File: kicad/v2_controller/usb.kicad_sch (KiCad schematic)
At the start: 23 parts, among them J3 USB_C_Receptacle_USB2.0, J4 USB_C_Receptacle_USB2.0, U4 NCP167BMX330TBG, U5 USBLC6-2P6, U6 USBLC6-2P6, U7 CP2102N-Axx-xQFN24

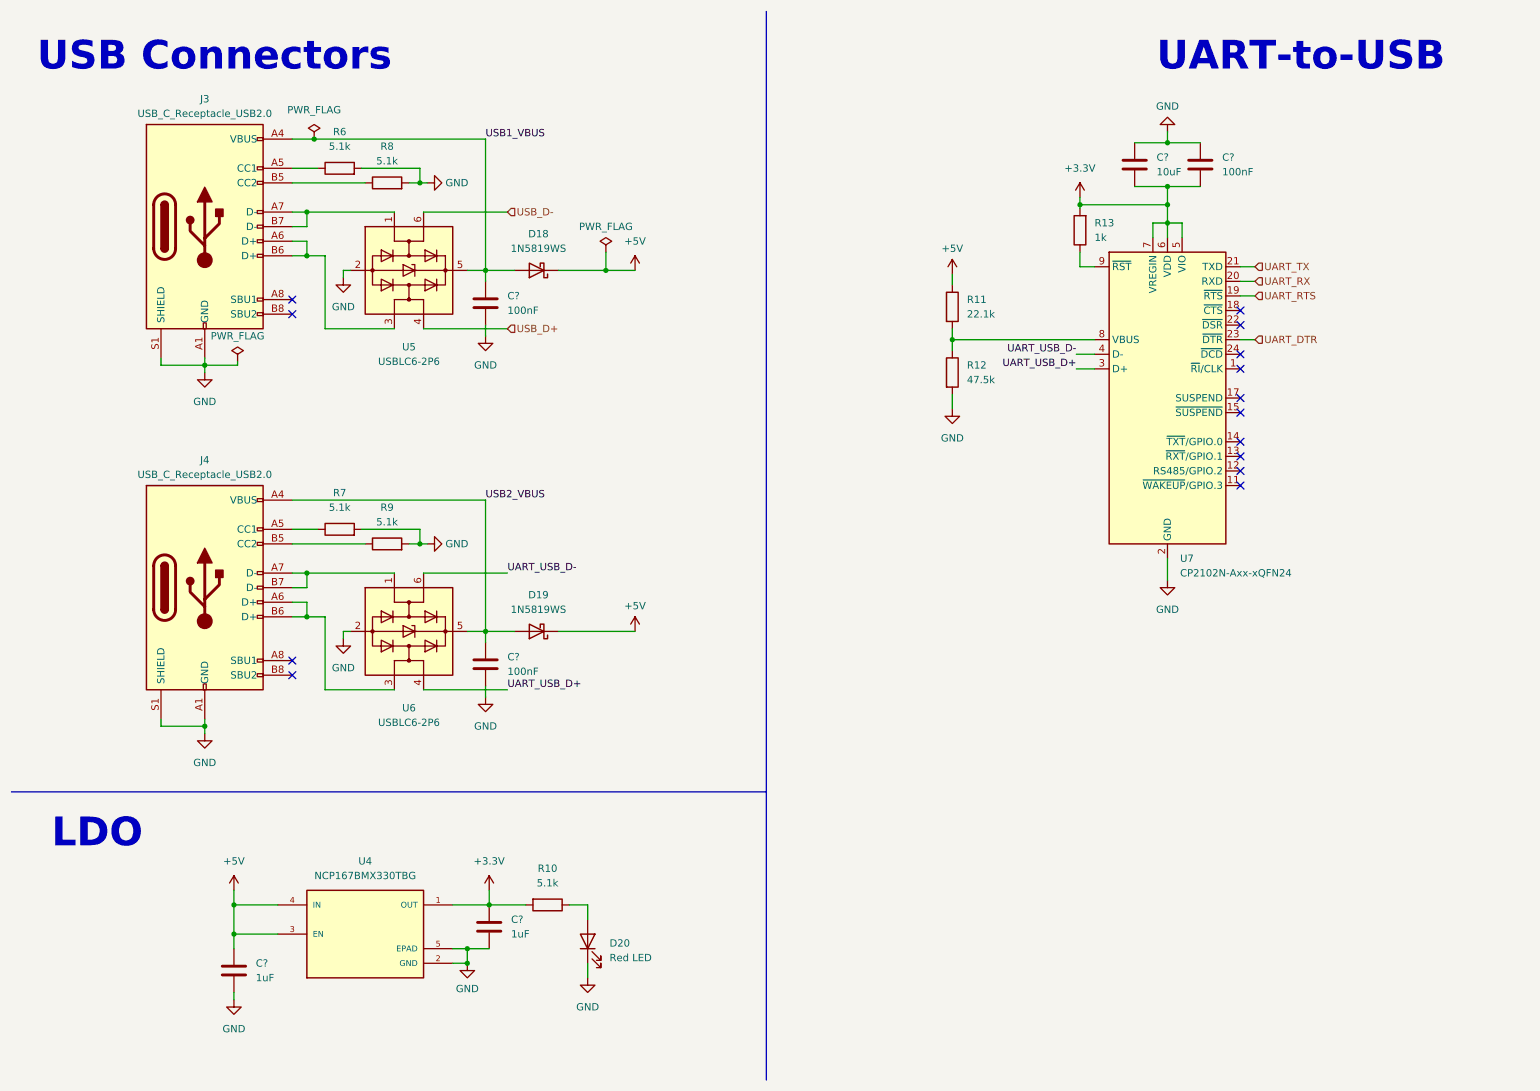
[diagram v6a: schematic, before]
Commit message: [kicad] finish initial component placement
This will probably need to be tweaked further once I begin routing,
but is a start for now.
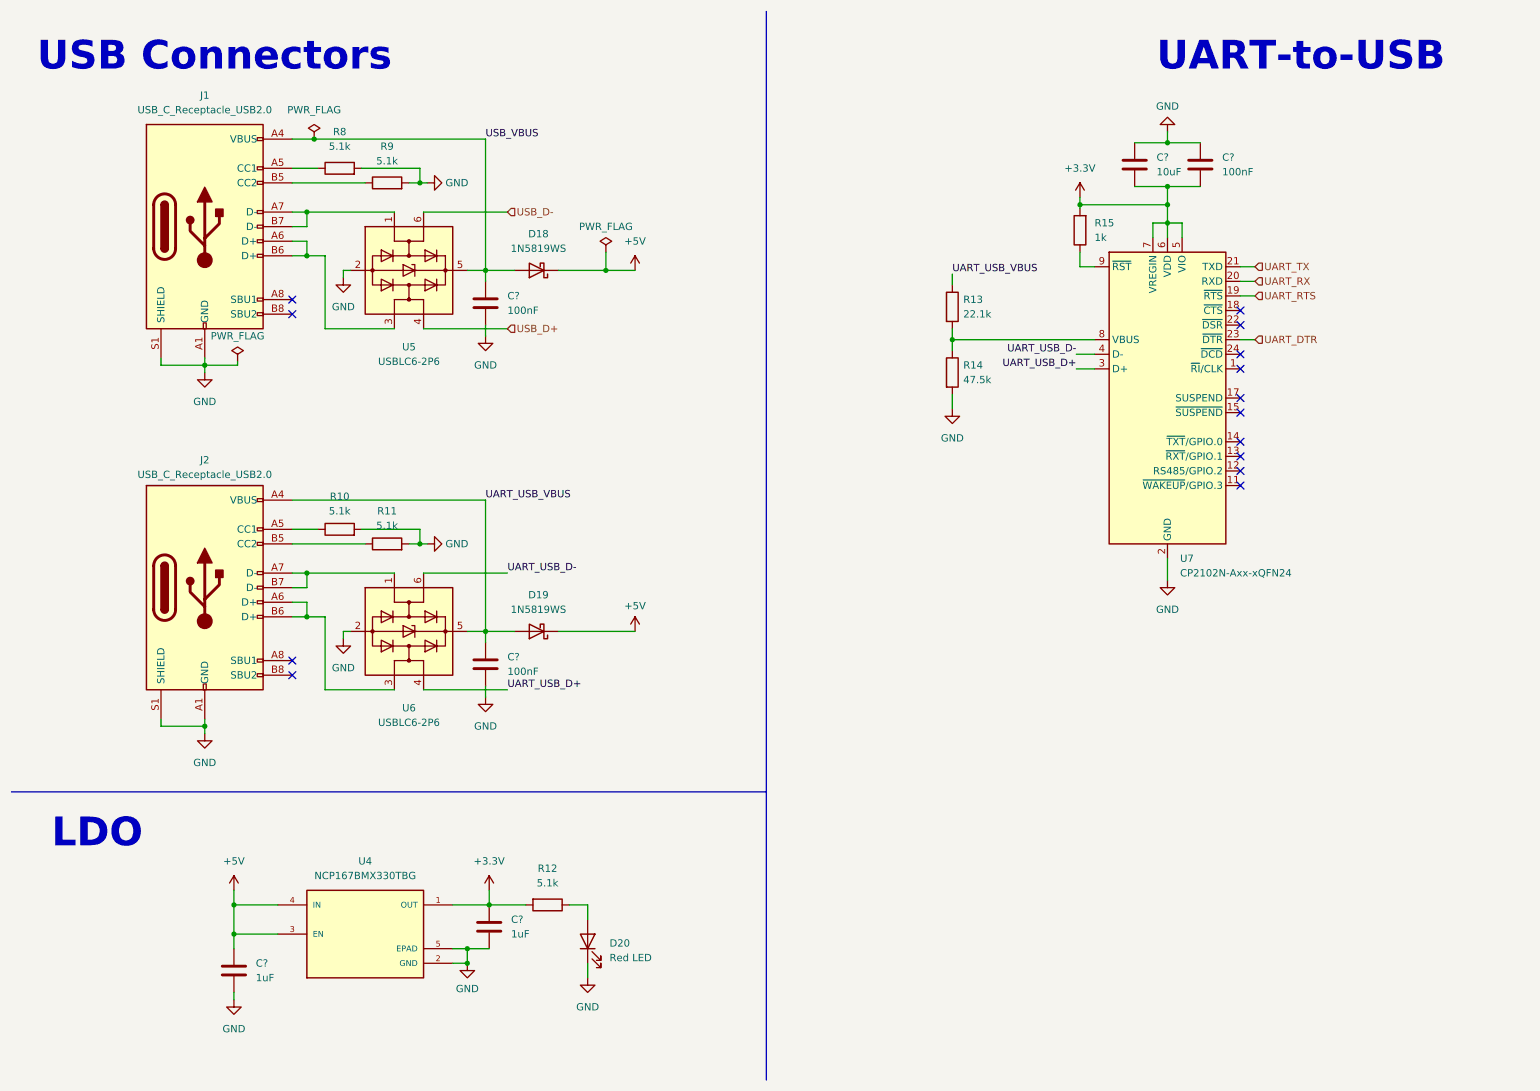
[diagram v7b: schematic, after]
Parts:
- U4: MANUFACTURER Onsemi -> (none); Manufacturer (none) -> Onsemi; Manufacturer Part # (none) -> NCP167BMX330TBG
- renumbered J3 to J1, J4 to J2, R7 to R10, R9 to R11, R10 to R12, R11 to R13, R12 to R14, R13 to R15, R6 to R8, R8 to R9
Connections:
- net +5V: no longer R13.1
- net USB1_VBUS renamed USB_VBUS
- net USB2_VBUS renamed UART_USB_VBUS
- net UART_USB_VBUS: now also R13.1

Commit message: [kicad] switch USB receptacles again, and other PCB improvements
Switch the USB receptacles to GT-USB-7090B, since the GT-USB-7051A had
very limited space for routing traces.

Also add labels on the key switches, and check in 3d models for more
components.
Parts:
- J1, J2: footprint Connector_USB:USB_C_Receptacle_G-Switch_GT-USB-7051x -> mantyl:GT-USB-7090x; LCSC Part # C2843970 -> C3019715; Manufacturer Part # (none) -> GT-USB-7090B
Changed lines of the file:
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@@
       (effects (font (size 1.27 1.27)))
     )
-    (property "Footprint" "Connector_USB:USB_C_Receptacle_G-Switch_GT-USB-7051x" (at 49.53 49.53 0)
-      (effects (font (size 1.27 1.27)) hide)
-    )
-    (property "Datasheet" "https://datasheet.lcsc.com/lcsc/2108072030_G-Switch-GT-USB-7051A_C2843970.pdf" (at 49.53 49.53 0)
-      (effects (font (size 1.27 1.27)) hide)
-    )
-    (property "LCSC Part #" "C2843970" (at 45.72 49.53 0)
-      (effects (font (size 1.27 1.27)) hide)
-    )
-    (property "Manufacturer Part #" "" (at 45.72 49.53 0)
+    (property "Footprint" "mantyl:GT-USB-7090x" (at 49.53 49.53 0)
+      (effects (font (size 1.27 1.27)) hide)
+    )
+    (property "Datasheet" "https://datasheet.lcsc.com/lcsc/2206021145_G-Switch-GT-USB-7090B_C3019715.pdf" (at 49.53 49.53 0)
+      (effects (font (size 1.27 1.27)) hide)
+    )
+    (property "LCSC Part #" "C3019715" (at 45.72 49.53 0)
+      (effects (font (size 1.27 1.27)) hide)
+    )
+    (property "Manufacturer Part #" "GT-USB-7090B" (at 45.72 49.53 0)
       (effects (font (size 1.27 1.27)) hide)
     )
@@
       (effects (font (size 1.27 1.27)))
     )
-    (property "Footprint" "Connector_USB:USB_C_Receptacle_G-Switch_GT-USB-7051x" (at 49.53 112.395 0)
-      (effects (font (size 1.27 1.27)) hide)
-    )
-    (property "Datasheet" "https://datasheet.lcsc.com/lcsc/2108072030_G-Switch-GT-USB-7051A_C2843970.pdf" (at 49.53 112.395 0)
-      (effects (font (size 1.27 1.27)) hide)
-    )
-    (property "LCSC Part #" "C2843970" (at 45.72 112.395 0)
-      (effects (font (size 1.27 1.27)) hide)
-    )
-    (property "Manufacturer Part #" "" (at 45.72 112.395 0)
-      (effects (font (size 1.27 1.27)) hide)
-    )
+    (property "Footprint" "mantyl:GT-USB-7090x" (at 49.53 112.395 0)
+      (effects (font (size 1.27 1.27)) hide)
+    )
+    (property "Datasheet" "https://datasheet.lcsc.com/lcsc/2206021145_G-Switch-GT-USB-7090B_C3019715.pdf" (at 49.53 112.395 0)
+      (effects (font (size 1.27 1.27)) hide)
+    )
+    (property "LCSC Part #" "C3019715" (at 45.72 112.395 0)
+      (effects (font (size 1.27 1.27)) hide)
+    )
+    (property "Manufacturer Part #" "GT-USB-7090B" (at 45.72 112.395 0)
+      (effects (font (size 1.27 1.27)) hide)
+    )
